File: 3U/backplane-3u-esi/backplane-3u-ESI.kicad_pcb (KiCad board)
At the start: 4 copper layers, 82.5 x 327 mm, 95 parts, among them J1 M55-6001642R

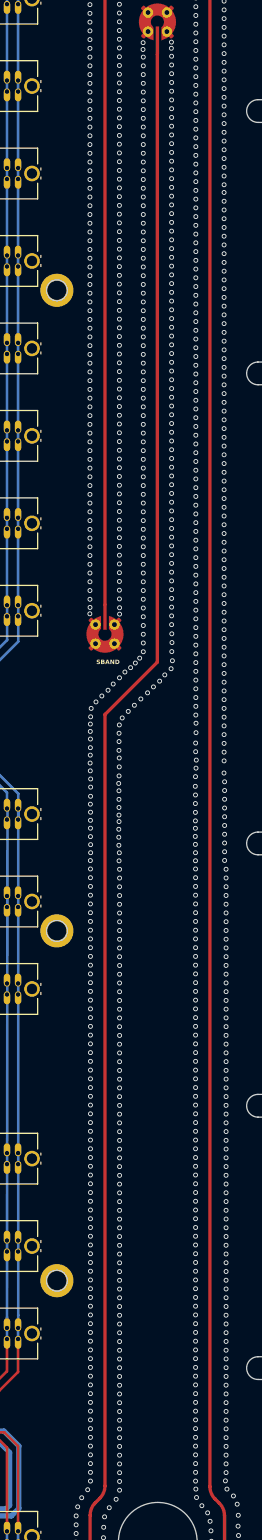
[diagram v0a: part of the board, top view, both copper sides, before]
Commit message: Final polishing of ESI backplane and updated Makefile
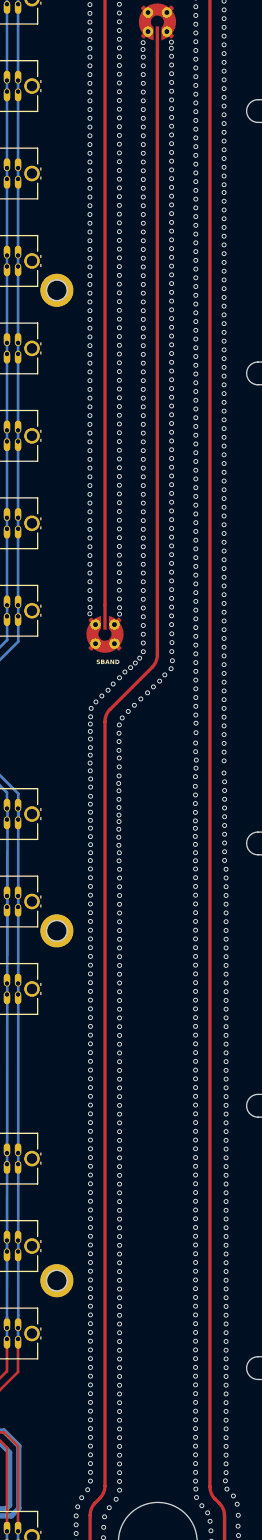
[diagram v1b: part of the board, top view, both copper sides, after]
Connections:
- net GPS-L1 renamed RF-GPS-L1
- net S-BAND renamed RF-S-BAND
- net UHF renamed RF-UHF
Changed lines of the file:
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@@
 	(net 9 "Net-(C20.1-Pad1)")
 	(net 10 "Net-(C20.2-Pad1)")
-	(net 11 "UHF")
+	(net 11 "RF-UHF")
 	(net 12 "OPD_PWR")
 	(net 13 "C3-UART-TX")
@@
 	(net 21 "MAG-SCL")
 	(net 22 "~{SD}")
-	(net 23 "S-BAND")
-	(net 24 "GPS-L1")
+	(net 23 "RF-S-BAND")
+	(net 24 "RF-GPS-L1")
 	(footprint "oresat-connectors:J-SAMTEC-SFM-120-X1-XXX-D"
 		(layer "F.Cu")
@@
 		(property ki_fp_filters "MountingHole*Pad*")
 		(sheetname "/")
-		(sheetfile "oresat-backplane-3u-ESI.kicad_sch")
+		(sheetfile "backplane-3u-ESI.kicad_sch")
 		(attr exclude_from_pos_files exclude_from_bom)
 		(fp_circle
@@
 		(property ki_fp_filters "MountingHole*Pad*")
 		(sheetname "/")
-		(sheetfile "oresat-backplane-3u-ESI.kicad_sch")
+		(sheetfile "backplane-3u-ESI.kicad_sch")
 		(attr exclude_from_pos_files exclude_from_bom)
 		(fp_circle
@@
 		(property ki_fp_filters "MountingHole*Pad*")
 		(sheetname "/")
-		(sheetfile "oresat-backplane-3u-ESI.kicad_sch")
+		(sheetfile "backplane-3u-ESI.kicad_sch")
 		(attr exclude_from_pos_files exclude_from_bom)
 		(fp_circle
@@
 		(property ki_fp_filters "MountingHole*Pad*")
 		(sheetname "/")
-		(sheetfile "oresat-backplane-3u-ESI.kicad_sch")
+		(sheetfile "backplane-3u-ESI.kicad_sch")
 		(attr exclude_from_pos_files exclude_from_bom)
 		(fp_circle
@@
 		(property ki_fp_filters "MountingHole*Pad*")
 		(sheetname "/")
-		(sheetfile "oresat-backplane-3u-ESI.kicad_sch")
+		(sheetfile "backplane-3u-ESI.kicad_sch")
 		(attr exclude_from_pos_files exclude_from_bom)
 		(fp_circle
@@
 		)
 		(sheetname "/RF Connectors/")
-		(sheetfile "oresat-backplane-3u-sch-rf3.kicad_sch")
+		(sheetfile "oresat-backplane-3u-sch-rf.kicad_sch")
 		(fp_rect
 			(start 1.2 -2.3)
@@
 			)
 			(layers "F.Cu")
-			(net 24 "GPS-L1")
+			(net 24 "RF-GPS-L1")
 			(pinfunction "RF")
 			(pintype "passive")
@@
 		(property ki_fp_filters "MountingHole*Pad*")
 		(sheetname "/")
-		(sheetfile "oresat-backplane-3u-ESI.kicad_sch")
+		(sheetfile "backplane-3u-ESI.kicad_sch")
 		(attr exclude_from_pos_files exclude_from_bom)
 		(fp_circle
@@
 		)
 		(sheetname "/RF Connectors/")
-		(sheetfile "oresat-backplane-3u-sch-rf3.kicad_sch")
+		(sheetfile "oresat-backplane-3u-sch-rf.kicad_sch")
 		(fp_rect
 			(start 1.2 -2.3)
@@
 			)
 			(layers "F.Cu")
-			(net 11 "UHF")
+			(net 11 "RF-UHF")
 			(pinfunction "RF")
 			(pintype "passive")
@@
 		)
 		(sheetname "/RF Connectors/")
-		(sheetfile "oresat-backplane-3u-sch-rf3.kicad_sch")
+		(sheetfile "oresat-backplane-3u-sch-rf.kicad_sch")
 		(fp_rect
 			(start 1.2 -2.3)
@@
 			)
 			(layers "F.Cu")
-			(net 23 "S-BAND")
+			(net 23 "RF-S-BAND")
 			(pinfunction "RF")
 			(pintype "passive")
@@
 		(property ki_fp_filters "MountingHole*Pad*")
 		(sheetname "/")
-		(sheetfile "oresat-backplane-3u-ESI.kicad_sch")
+		(sheetfile "backplane-3u-ESI.kicad_sch")
 		(attr exclude_from_pos_files exclude_from_bom)
 		(fp_circle
@@
 		)
 		(sheetname "/RF Connectors/")
-		(sheetfile "oresat-backplane-3u-sch-rf3.kicad_sch")
+		(sheetfile "oresat-backplane-3u-sch-rf.kicad_sch")
 		(fp_rect
 			(start 1.2 -2.3)
@@
 			)
 			(layers "F.Cu")
-			(net 24 "GPS-L1")
+			(net 24 "RF-GPS-L1")
 			(pinfunction "RF")
 			(pintype "passive")
@@
 		(property ki_fp_filters "MountingHole*Pad*")
 		(sheetname "/")
-		(sheetfile "oresat-backplane-3u-ESI.kicad_sch")
+		(sheetfile "backplane-3u-ESI.kicad_sch")
 		(attr exclude_from_pos_files exclude_from_bom)
 		(fp_circle
@@
 		)
 		(sheetname "/RF Connectors/")
-		(sheetfile "oresat-backplane-3u-sch-rf3.kicad_sch")
+		(sheetfile "oresat-backplane-3u-sch-rf.kicad_sch")
 		(fp_rect
 			(start 1.2 -2.3)
@@
 			)
 			(layers "F.Cu")
-			(net 11 "UHF")
+			(net 11 "RF-UHF")
 			(pinfunction "RF")
 			(pintype "passive")
@@
 		(property ki_fp_filters "MountingHole*Pad*")
 		(sheetname "/")
-		(sheetfile "oresat-backplane-3u-ESI.kicad_sch")
+		(sheetfile "backplane-3u-ESI.kicad_sch")
 		(attr exclude_from_pos_files exclude_from_bom)
 		(fp_circle
@@
 		)
 		(sheetname "/RF Connectors/")
-		(sheetfile "oresat-backplane-3u-sch-rf3.kicad_sch")
+		(sheetfile "oresat-backplane-3u-sch-rf.kicad_sch")
 		(fp_rect
 			(start 1.2 -2.3)
@@
 			)
 			(layers "F.Cu")
-			(net 23 "S-BAND")
+			(net 23 "RF-S-BAND")
 			(pinfunction "RF")
 			(pintype "passive")
@@
 		(property ki_fp_filters "MountingHole*Pad*")
 		(sheetname "/")
-		(sheetfile "oresat-backplane-3u-ESI.kicad_sch")
+		(sheetfile "backplane-3u-ESI.kicad_sch")
 		(attr exclude_from_pos_files exclude_from_bom)
 		(fp_circle
@@
 		(property ki_fp_filters "MountingHole*Pad*")
 		(sheetname "/")
-		(sheetfile "oresat-backplane-3u-ESI.kicad_sch")
+		(sheetfile "backplane-3u-ESI.kicad_sch")
 		(attr exclude_from_pos_files exclude_from_bom)
 		(fp_circle
@@
 		(property ki_fp_filters "MountingHole*Pad*")
 		(sheetname "/")
-		(sheetfile "oresat-backplane-3u-ESI.kicad_sch")
+		(sheetfile "backplane-3u-ESI.kicad_sch")
 		(attr exclude_from_pos_files exclude_from_bom)
 		(fp_circle
@@
 	)
 	(gr_circle
-		(center 334.694589 251.8284)
-		(end 339.855 249.7964)
+		(center 334.738 251.8117)
+		(end 339.2 251.85)
 		(stroke
 			(width 0.5)
 			(type default)
 		)
-		(fill no)
+		(fill yes)
+		(locked yes)
 		(layer "F.Mask")
 	)
@@
 		(layer "B.Mask")
 	)
+	(gr_circle
+		(center 334.738 251.8)
+		(end 339.2 251.8383)
+		(stroke
+			(width 0.5)
+			(type solid)
+		)
+		(fill yes)
+		(locked yes)
+		(layer "B.Mask")
+	)
 	(gr_poly
 		(pts
@@
 	)
 	(segment
-		(start 328.7 157.2)
-		(end 334.69 151.21)
+		(start 329.285787 156.614213)
+		(end 334.104214 151.795786)
 		(width 0.38)
 		(layer "F.Cu")
@@
 	(segment
 		(start 328.7 245.416373)
-		(end 328.7 157.2)
+		(end 328.7 158.028427)
 		(width 0.38)
 		(layer "F.Cu")
@@
 	)
 	(segment
-		(start 334.69 151.21)
+		(start 334.69 150.381573)
 		(end 334.69 81.69)
 		(width 0.38)
@@
 	)
 	(arc
+		(start 334.104214 151.795786)
+		(mid 334.537759 151.14694)
+		(end 334.69 150.381573)
+		(width 0.38)
+		(layer "F.Cu")
+		(net 24)
+	)
+	(arc
 		(start 328.114213 256.978613)
 		(mid 328.547759 257.62746)
@@
 		(width 0.38)
 		(layer "F.Cu")
+		(net 24)
+	)
+	(arc
+		(start 329.285787 156.614213)
+		(mid 328.852241 157.26306)
+		(end 328.7 158.028427)
+		(width 0.38)
+		(layer "F.Cu")
